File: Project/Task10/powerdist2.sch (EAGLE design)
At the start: 50 parts

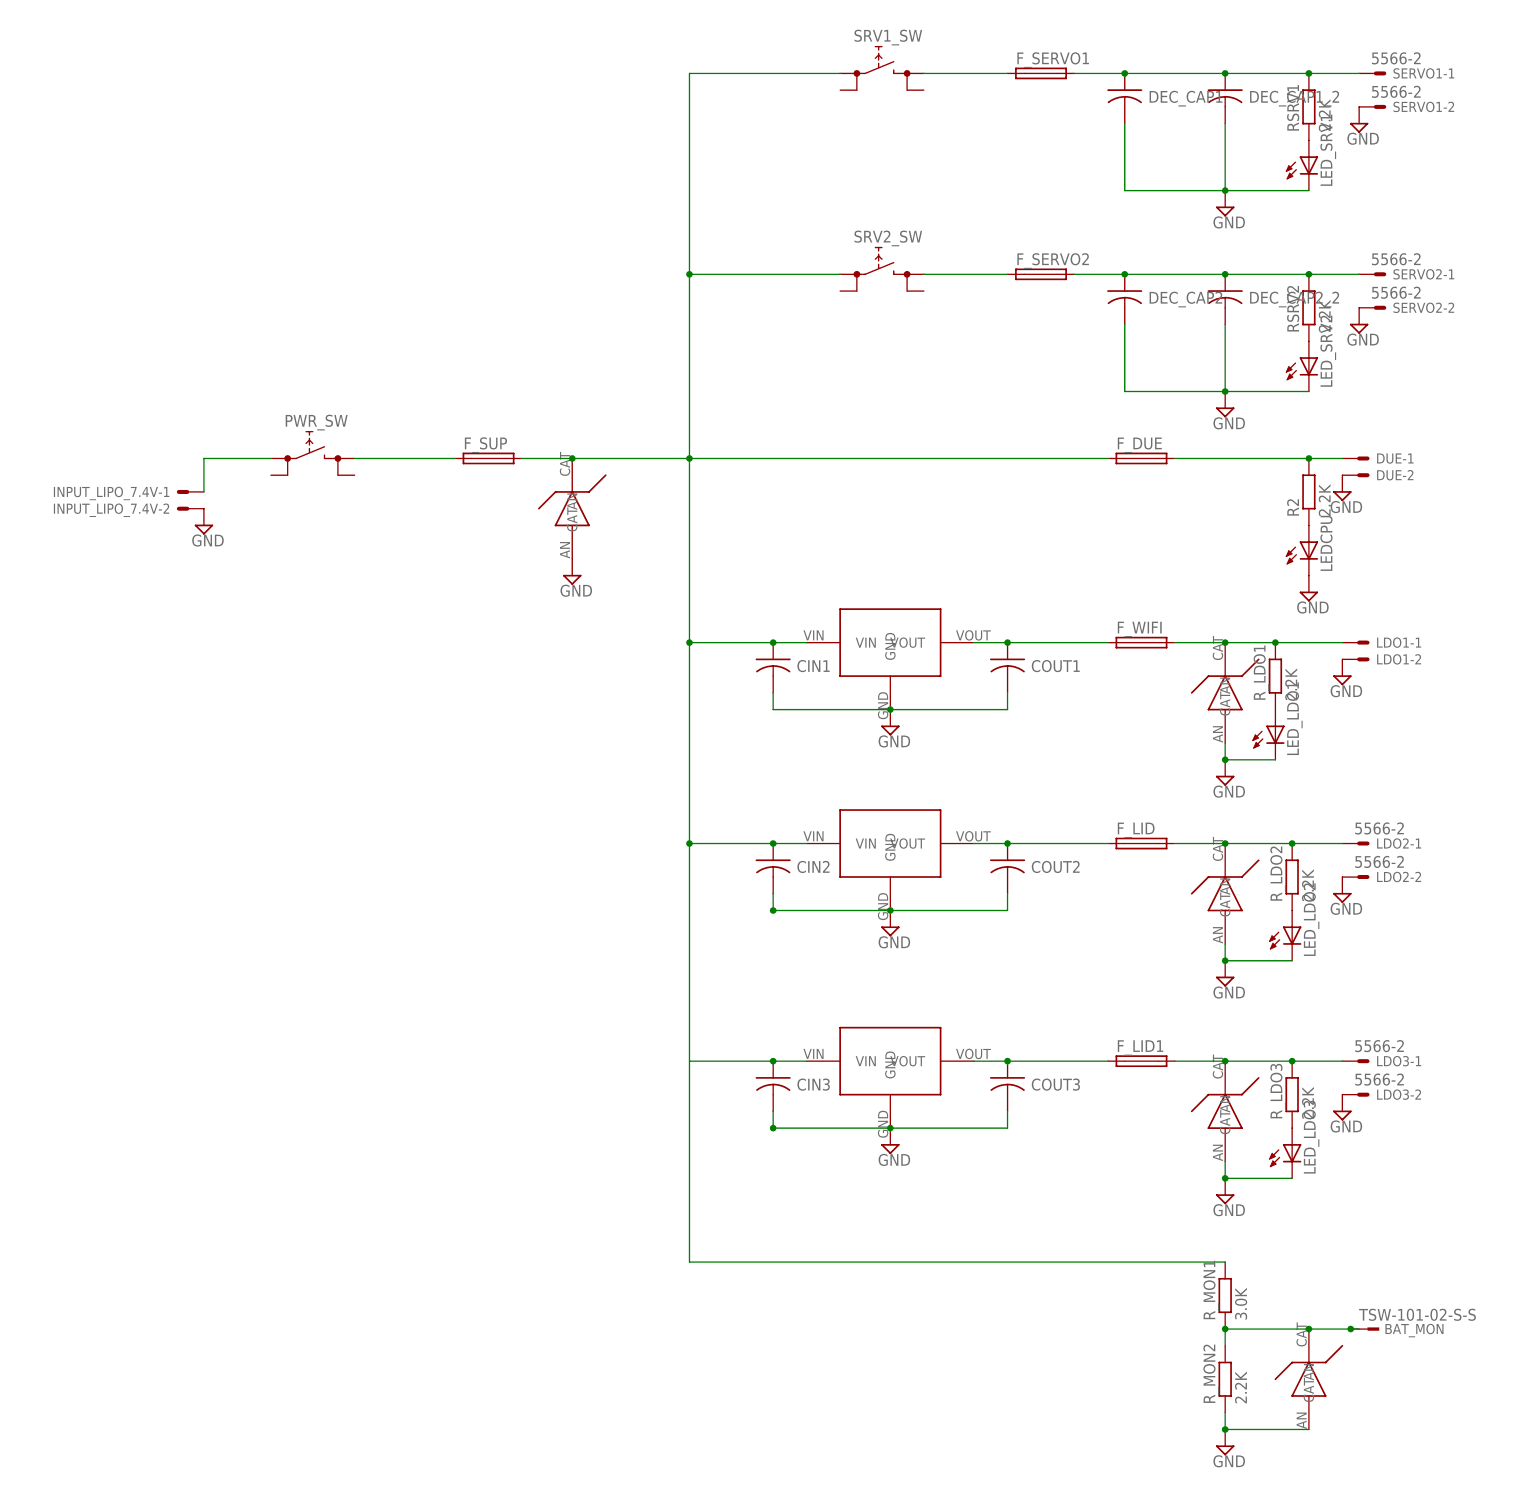
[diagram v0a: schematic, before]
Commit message: Updated power distribution board schematic
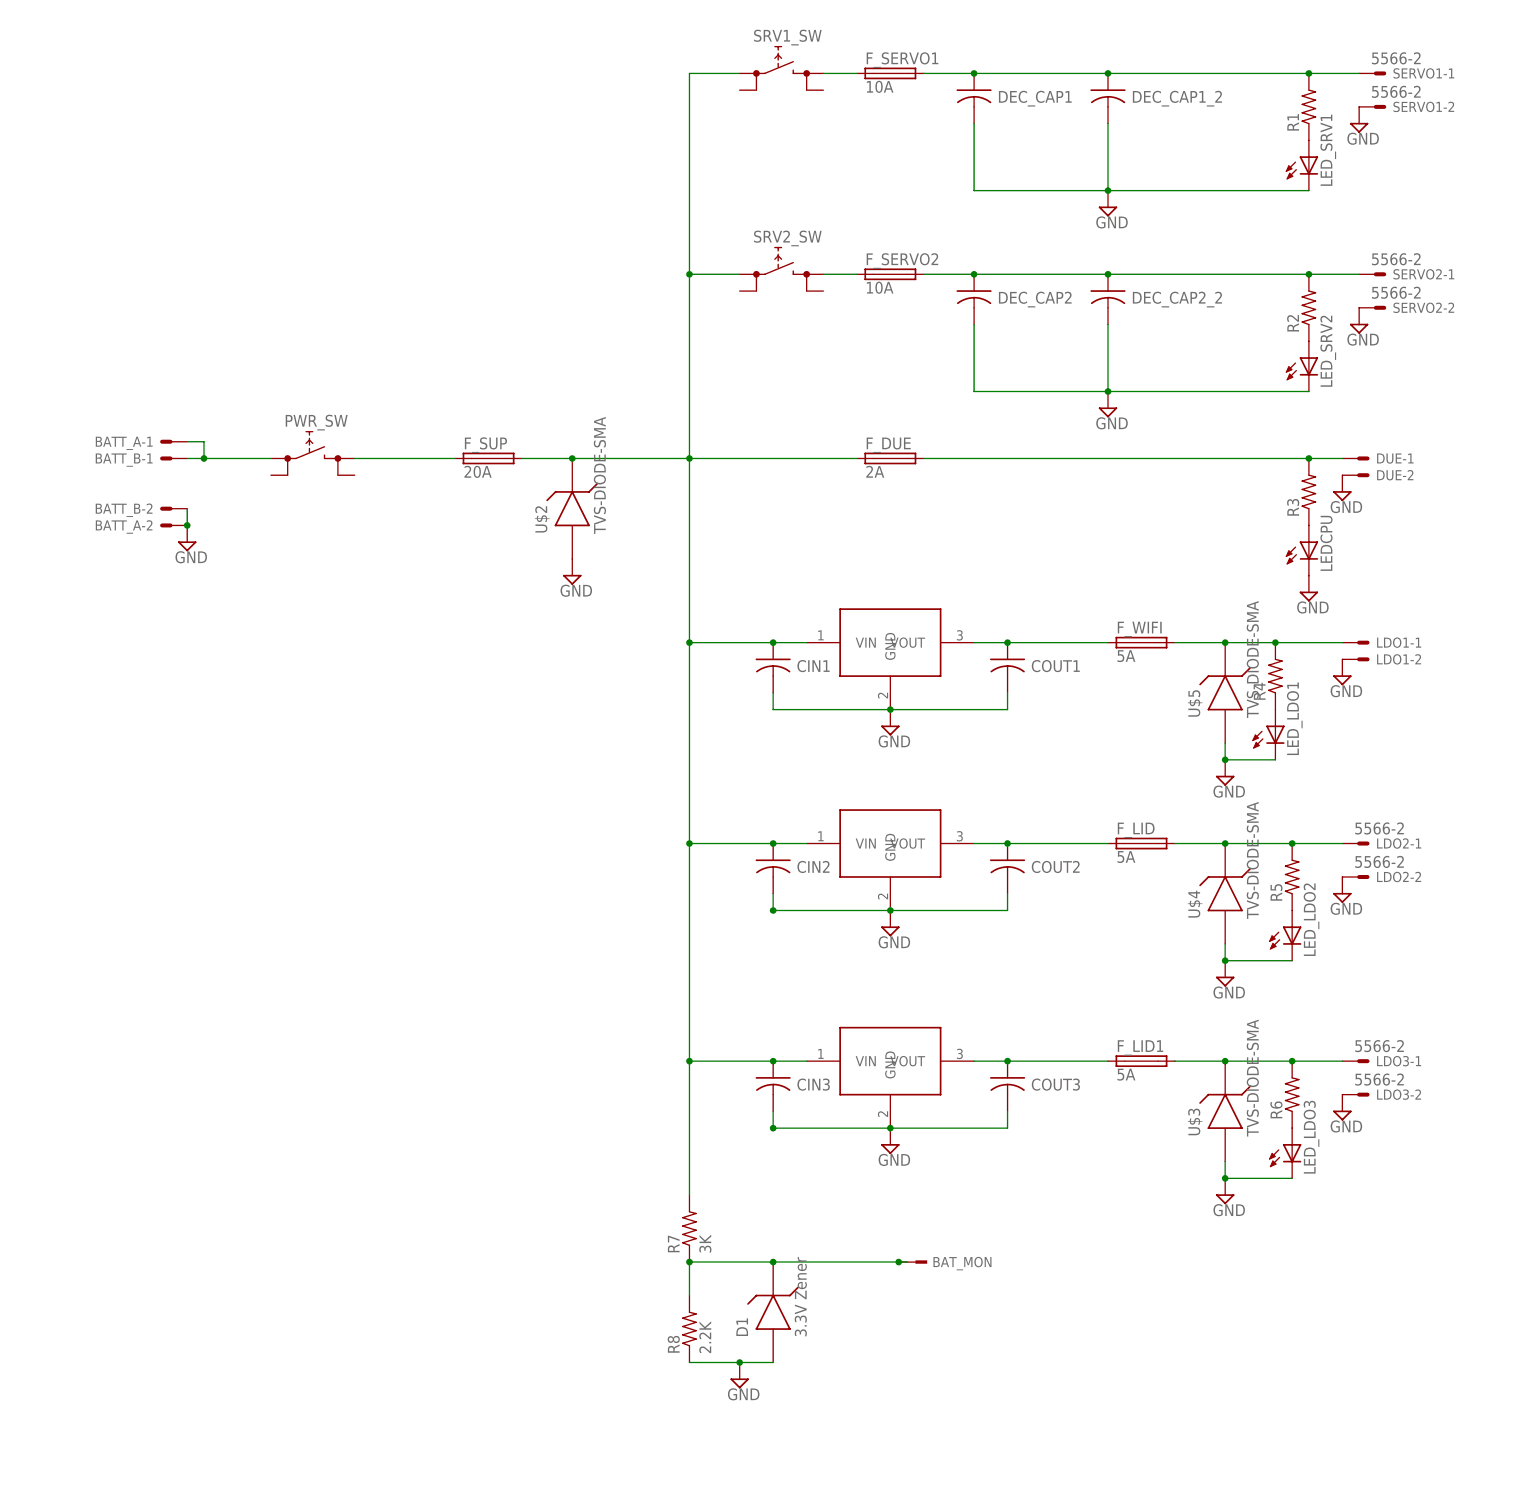
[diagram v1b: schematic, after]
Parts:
- removed INPUT_LIPO_7.4V: 22-23-2021, con-molex:22-23-2021
- removed LID12V1A, LID12V1A1, WIFI5V1A1: MIC29150/29300/29500, Micrel-Voltage-Regulator:MIC29150/29300/29500
- removed RSRV1, RSRV2, R_LDO1, R_LDO2, R_LDO3, R_MON2: 2.2K, resistor:R-EU_R0402
- removed R_MON1: 3.0K, resistor:R-EU_R0402
- removed TVS-MAIN: 26V, Micrel-Voltage-Regulator:TVS-DIODE-SMAJ
- removed TVS-MAIN1, TVS-MAIN3, TVS_3.3: 16V, Micrel-Voltage-Regulator:TVS-DIODE-SMAJ
- removed TVS-MAIN2: 5V, Micrel-Voltage-Regulator:TVS-DIODE-SMAJ
- added BATT_A, BATT_B: 22-23-2021, con-molex:22-23-2021
- added D1: 3.3V Zener, Task5:TVS-DIODE-SMA
- added R1, R3, R4, R5, R6: (no value), rcl:R-US_0309/10
- added R7: 3K, rcl:R-US_0309/10
- added R8: 2.2K, rcl:R-US_0309/10
- added U$1, U$6, U$7: MIC29150/29300/29500, Task5:MIC29150/29300/29500
- added U$2, U$3, U$4, U$5: TVS-DIODE-SMA, Task5:TVS-DIODE-SMA
- F_DUE: value (none) -> 2A
- F_LID, F_LID1, F_WIFI: value (none) -> 5A
- F_SERVO1, F_SERVO2: value (none) -> 10A
- F_SUP: value (none) -> 20A
- R2: value 2.2K -> (none); device resistor:R-EU_R0402 -> rcl:R-US_0309/10
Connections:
- removed net N$12: CIN1.1, CIN2.1, F_DUE.1, F_SUP.2, LID12V1A.VIN, R_MON1.2, SRV1_SW.0@A, SRV2_SW.0@A, TVS-MAIN.CAT, WIFI5V1A1.VIN
- net GND: now also BATT_A-2.S, BATT_B-2.S, D1.AN, R8.1, U$1.GND, U$2.AN, U$3.AN, U$4.AN, U$5.AN, U$6.GND, U$7.GND; no longer INPUT_LIPO_7.4V-2.S, LID12V1A.GND, LID12V1A1.GND, R_MON2.1, TVS-MAIN.AN, TVS-MAIN1.AN, TVS-MAIN2.AN, TVS-MAIN3.AN, TVS_3.3.AN, WIFI5V1A1.GND
- net N$1: now also R2.2; no longer RSRV2.2
- net N$10: now also BATT_A-1.S, BATT_B-1.S; no longer INPUT_LIPO_7.4V-1.S
- net N$11: now also LEDCPU.A, R3.1; no longer LED_LDO1.A, R_LDO1.1
- net N$13: now also LED_LDO1.A, R4.1; no longer LED_LDO2.A, R_LDO2.1
- net N$15: now also R1.2; no longer RSRV1.2
- net N$16: now also LED_LDO2.A, R5.1; no longer LED_SRV1.A, RSRV1.1
- net N$18: now also D1.CAT, R7.1, R8.2; no longer R_MON1.1, R_MON2.2, TVS_3.3.CAT
- net N$19: now also U$1.VOUT; no longer LID12V1A1.VOUT
- net N$2: now also R5.2, U$4.CAT; no longer R_LDO2.2, TVS-MAIN3.CAT
- net N$20: now also CIN1.1, CIN2.1, F_DUE.1, F_SUP.2, R7.2, SRV1_SW.0@A, SRV2_SW.0@A, U$1.VIN, U$2.CAT, U$6.VIN, U$7.VIN; no longer LID12V1A1.VIN
- net N$21: now also R6.2, U$3.CAT; no longer R_LDO3.2, TVS-MAIN1.CAT
- net N$22: now also R6.1; no longer R_LDO3.1
- net N$4: now also R3.2; no longer R2.2
- net N$5: now also LED_SRV1.A, R1.1; no longer LED_SRV2.A, RSRV2.1
- net N$6: now also U$7.VOUT; no longer WIFI5V1A1.VOUT
- net N$7: now also R4.2, U$5.CAT; no longer R_LDO1.2, TVS-MAIN2.CAT
- net N$8: now also LED_SRV2.A; no longer LEDCPU.A
- net N$9: now also U$6.VOUT; no longer LID12V1A.VOUT
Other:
- moved on the sheet: BAT_MON, DEC_CAP1, DEC_CAP1_2, DEC_CAP2, DEC_CAP2_2, F_DUE, F_SERVO1, F_SERVO2, SRV1_SW, SRV2_SW

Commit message: Updated Schematic, ready for submitting...
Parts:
- removed DEC_CAP1, DEC_CAP1_2, DEC_CAP2, DEC_CAP2_2: CAPACITORTH_CAP, TinyGadget(1):CAPACITORTH_CAP
- removed LDO1: C-GRID-02-70553, con-molex:C-GRID-02-70553
- removed LDO2, LDO3: 5566-2, con-molex:5566-2
- removed LEDCPU, LED_LDO1, LED_LDO2, LED_LDO3, LED_SRV1, LED_SRV2: (no value), led:LEDCHIP-LED0805
- removed PWR_SW, SRV1_SW, SRV2_SW: (no value), switch:REKN
- added ACC1: C-GRID-02-70553, con-molex:C-GRID-02-70553
- added ACC2, ACC3: 5566-2, con-molex:5566-2
- added C1, C2, C3, C4: CAPACITORTH_CAP, TinyGadget(1):CAPACITORTH_CAP
- added LED1, LED2, LED3, LED4, LED5, LED6: (no value), led:LEDCHIP-LED0805
- added S1: (no value), switch:255SB
- R1, R2, R3, R4, R5, R6: value (none) -> 1K
- U$2: value TVS-DIODE-SMA -> 8V
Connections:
- removed net N$17: F_SERVO2.1, SRV2_SW.1@A
- removed net N$20: CIN1.1, CIN2.1, CIN3.1, F_DUE.1, F_SUP.2, R7.2, SRV1_SW.0@A, SRV2_SW.0@A, U$1.VIN, U$2.CAT, U$6.VIN, U$7.VIN
- removed net N$3: F_SERVO1.1, SRV1_SW.1@A
- new net V_SUPPLY: CIN1.1, CIN2.1, CIN3.1, F_DUE.1, F_SERVO1.1, F_SERVO2.1, F_SUP.2, R7.2, U$1.VIN, U$2.CAT, U$6.VIN, U$7.VIN
- net GND: now also ACC1-2.S, ACC2-2.S, ACC3-2.S, C1.2, C2.2, C3.2, C4.2, LED1.C, LED2.C, LED3.C, LED4.C, LED5.C, LED6.C; no longer DEC_CAP1.2, DEC_CAP1_2.2, DEC_CAP2.2, DEC_CAP2_2.2, LDO1-2.S, LDO2-2.S, LDO3-2.S, LEDCPU.C, LED_LDO1.C, LED_LDO2.C, LED_LDO3.C, LED_SRV1.C, LED_SRV2.C
- net N$1: now also C3.1, C4.1; no longer DEC_CAP2.1, DEC_CAP2_2.1
- net N$10: now also S1.P; no longer PWR_SW.0@A
- net N$11: now also LED4.A; no longer LEDCPU.A
- net N$13: now also LED1.A; no longer LED_LDO1.A
- net N$14: now also S1.O; no longer PWR_SW.1@A
- net N$15: now also C1.1, C2.1; no longer DEC_CAP1.1, DEC_CAP1_2.1
- net N$16: now also LED2.A; no longer LED_LDO2.A
- net N$2: now also ACC2-1.S; no longer LDO2-1.S
- net N$21: now also ACC3-1.S; no longer LDO3-1.S
- net N$22: now also LED3.A; no longer LED_LDO3.A
- net N$5: now also LED6.A; no longer LED_SRV1.A
- net N$7: now also ACC1-1.S; no longer LDO1-1.S
- net N$8: now also LED5.A; no longer LED_SRV2.A
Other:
- moved on the sheet: BATT_A-1, BATT_A-2, BATT_B-1, BATT_B-2, BAT_MON, CIN1, CIN2, CIN3, COUT1, COUT2, COUT3, D1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
